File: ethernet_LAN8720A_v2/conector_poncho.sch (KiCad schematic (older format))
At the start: 1 part

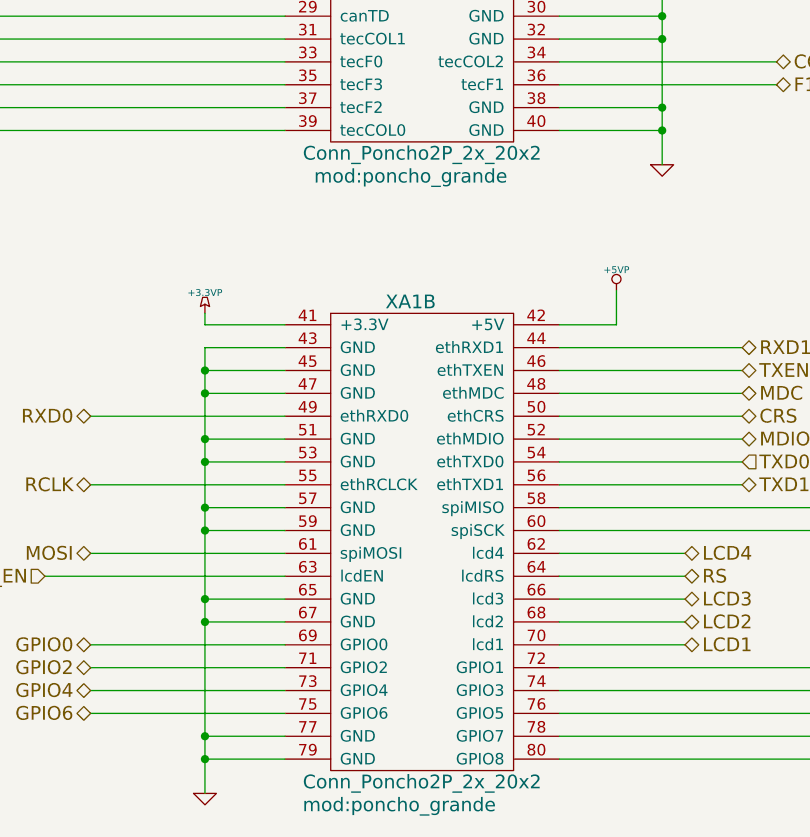
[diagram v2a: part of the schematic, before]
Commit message: Asocio footprints y realizo un placement MUY preliminar.
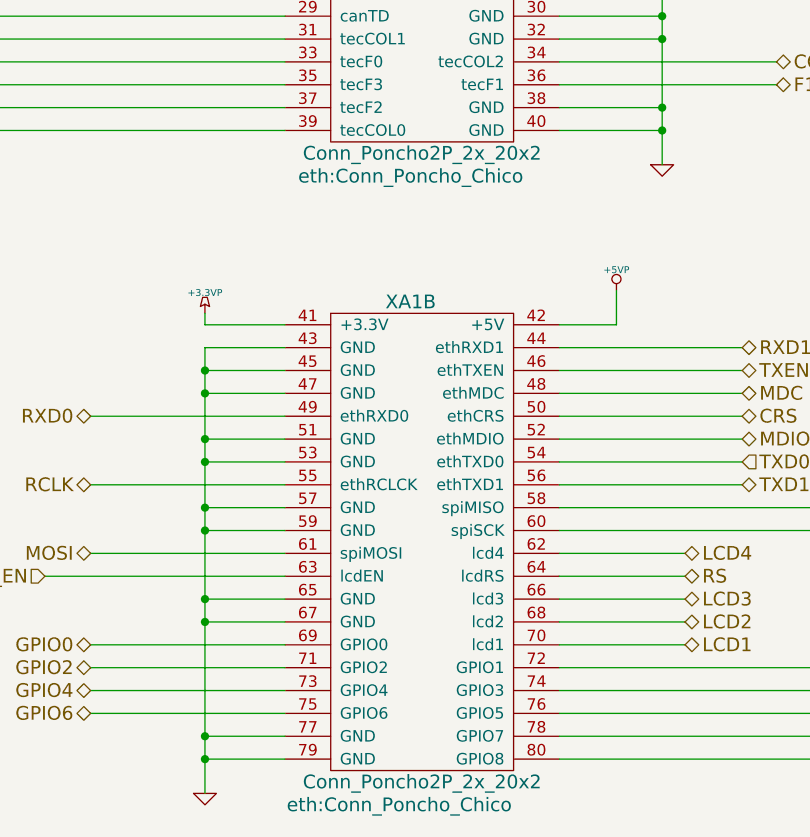
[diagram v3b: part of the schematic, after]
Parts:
- XA1: footprint mod:poncho_grande -> eth:Conn_Poncho_Chico
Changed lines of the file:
@@
 F 0 "XA1" H 5650 4650 60  0000 C CNN
 F 1 "Conn_Poncho2P_2x_20x2" H 5700 2550 60  0000 C CNN
-F 2 "mod:poncho_grande" H 5600 2450 60  0000 C CNN
+F 2 "eth:Conn_Poncho_Chico" H 5600 2450 60  0000 C CNN
 F 3 "" H 5350 4250 60  0000 C CNN
 	2    5350 4250
@@
 F 0 "XA1" H 5650 1900 60  0000 C CNN
 F 1 "Conn_Poncho2P_2x_20x2" H 5700 -200 60  0000 C CNN
-F 2 "mod:poncho_grande" H 5650 -300 60  0000 C CNN
+F 2 "eth:Conn_Poncho_Chico" H 5650 -300 60  0000 C CNN
 F 3 "" H 5350 1500 60  0000 C CNN
 	1    5350 1500

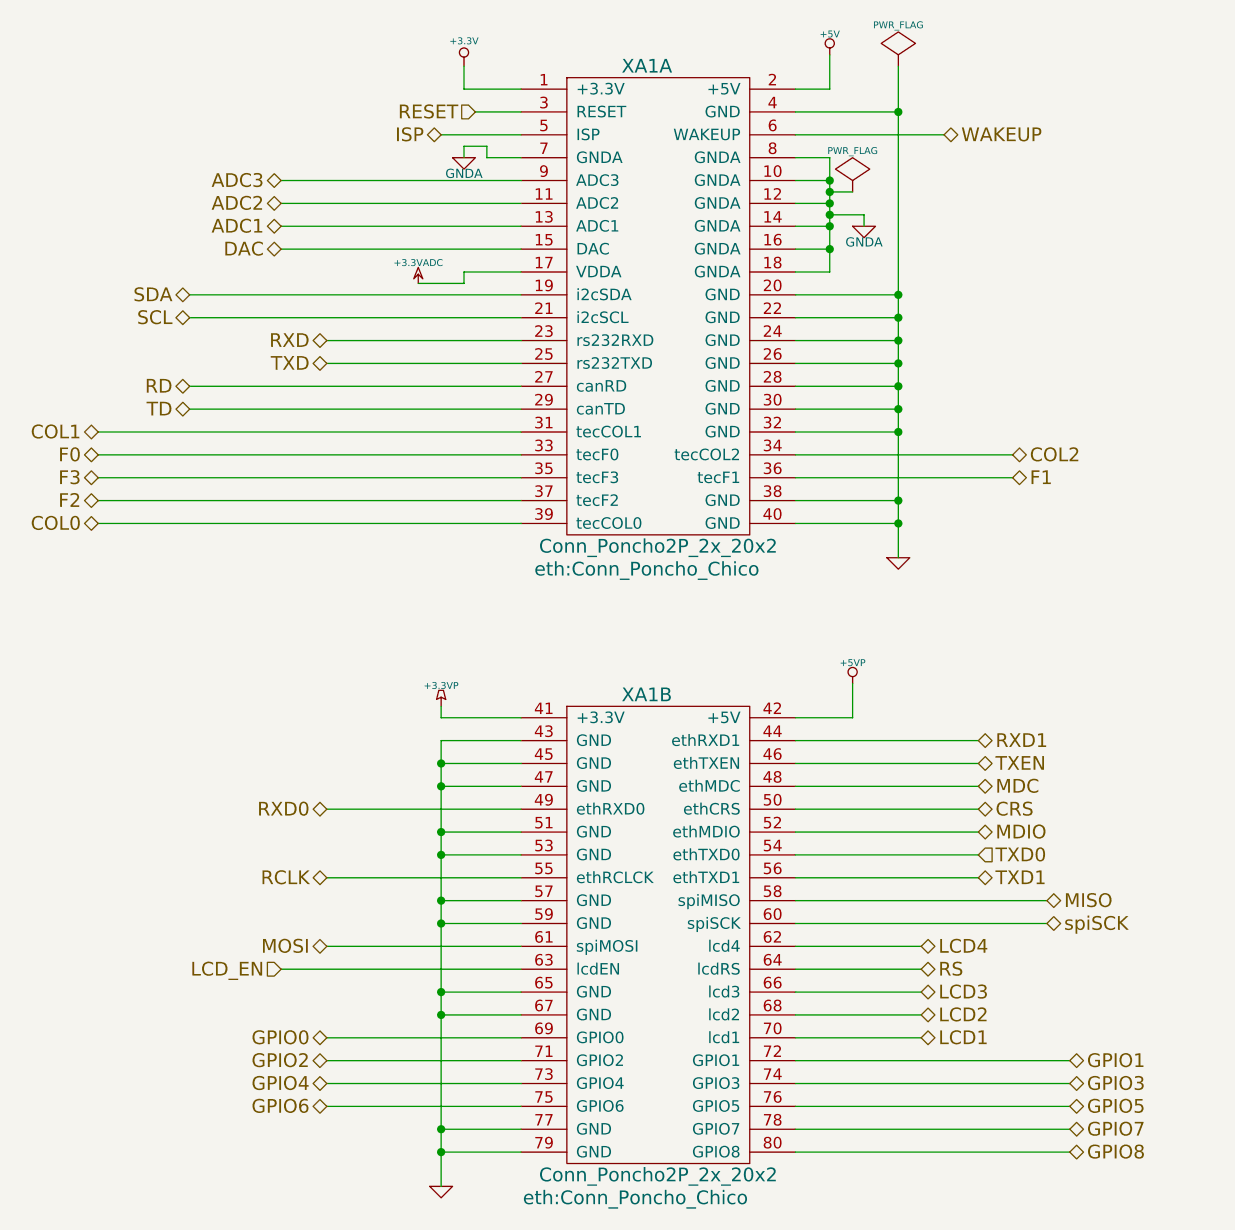
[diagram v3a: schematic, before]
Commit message: Modifico el Poncho ETH para que sea solo Poncho Izquierdo.
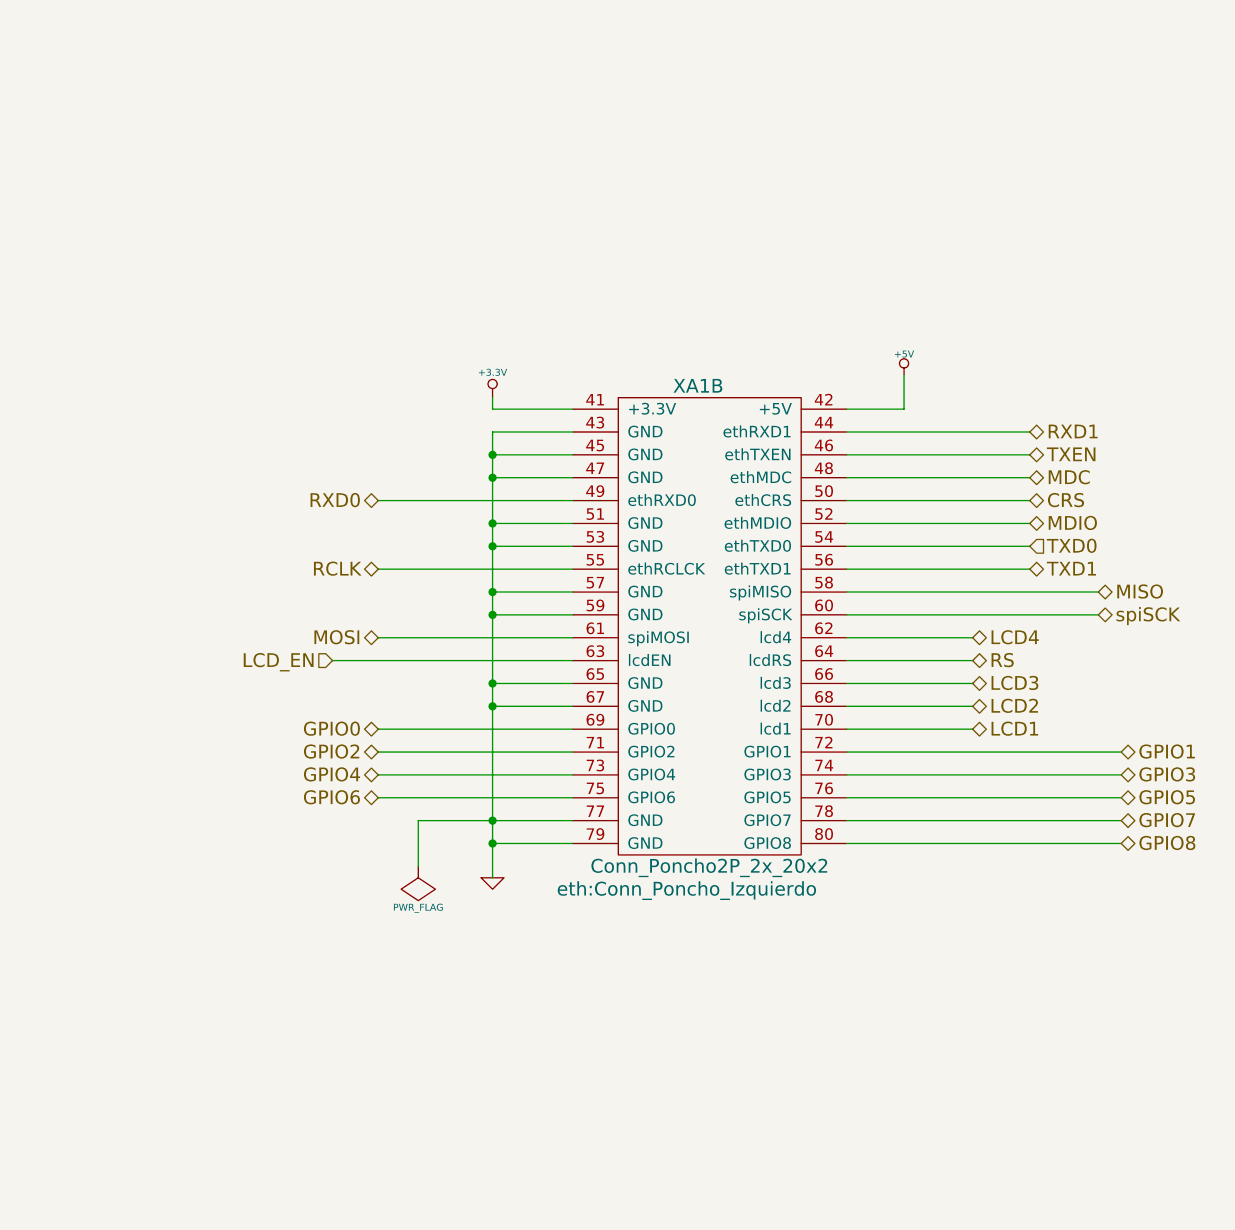
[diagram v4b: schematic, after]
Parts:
- removed unit 1 of XA1
- XA1: footprint eth:Conn_Poncho_Chico -> eth:Conn_Poncho_Izquierdo
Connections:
- net +3.3VP is gone; now on net +3.3V: XA1.41 (+3.3V)
- net +5VP is gone; now on net +5V: XA1.42 (+5V)
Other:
- moved on the sheet: XA1B
